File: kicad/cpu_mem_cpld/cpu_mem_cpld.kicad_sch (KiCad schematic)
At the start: 47 parts, among them CON1 BARREL_JACK, J1 USB, J3 DB9, SW1 SW_PUSH, U1 W65C02SxPL, U10 74HC245, U11 16550, U13 MAX232, U2 XC95108PC84, U3 28C256, U4 IS61C5128AS-25QLI, U5 74LS06, U6 LM555N, U9 74HC245, X1 OSC, X2 OSC

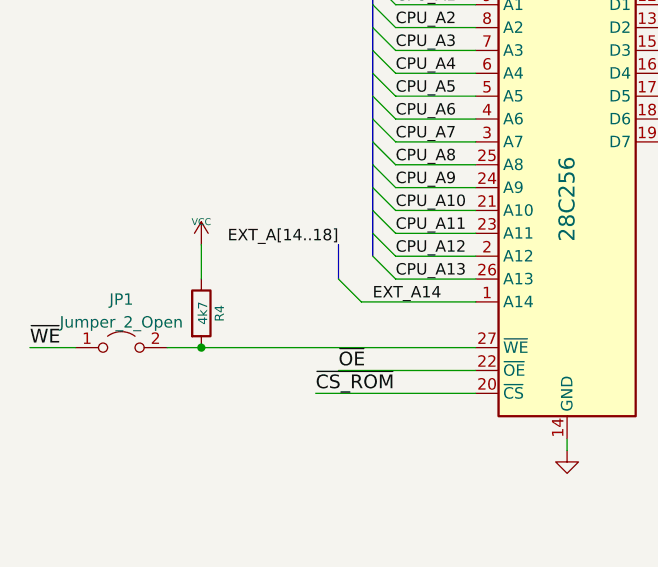
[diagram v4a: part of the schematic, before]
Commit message: eeprom rw jumper
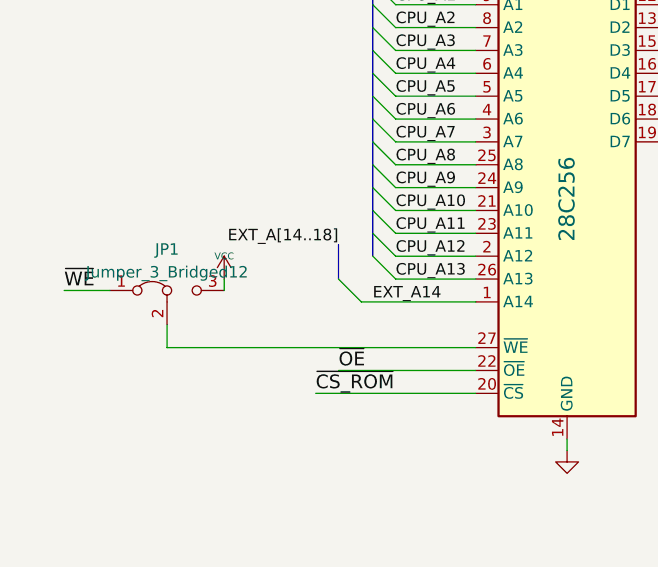
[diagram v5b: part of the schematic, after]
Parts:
- removed JP1: Jumper_2_Open, Connector_PinHeader_2.54mm:PinHeader_2x01_P2.54mm_Vertical, symbol Jumper:Jumper_2_Open
- removed R4: 4k7, Resistor_THT:R_Axial_DIN0204_L3.6mm_D1.6mm_P5.08mm_Horizontal, symbol Device:R
- added JP1: Jumper_3_Bridged12, Connector_PinHeader_2.54mm:PinHeader_1x03_P2.54mm_Vertical, symbol Jumper:Jumper_3_Bridged12
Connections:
- net VCC: now also JP1.3 (B)
- net ~{WE}: now also JP1.1 (A)
- net at U3.27 (~{WE}): now also JP1.2 (C)
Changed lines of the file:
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@@
   (junction (at 58.42 275.59) (diameter 0) (color 0 0 0 0)
   )
-  (junction (at 31.75 204.47) (diameter 0) (color 0 0 0 0)
-  )
   (junction (at 100.33 267.97) (diameter 0) (color 0 0 0 0)
   )
@@
     (stroke (width 0) (type default) (color 0 0 0 0))
   )
-  (wire (pts (xy 31.75 204.47) (xy 62.23 204.47))
+  (wire (pts (xy 27.94 204.47) (xy 62.23 204.47))
     (stroke (width 0) (type default) (color 0 0 0 0))
   )
@@
     (stroke (width 0) (type default) (color 0 0 0 0))
   )
+  (wire (pts (xy 27.94 201.93) (xy 27.94 204.47))
+    (stroke (width 0) (type default) (color 0 0 0 0))
+  )
   (wire (pts (xy 140.97 259.08) (xy 167.64 259.08))
     (stroke (width 0) (type default) (color 0 0 0 0))
@@
     (stroke (width 0) (type default) (color 0 0 0 0))
   )
-  (wire (pts (xy 31.75 193.04) (xy 31.75 196.85))
+  (wire (pts (xy 34.29 196.85) (xy 34.29 198.12))
     (stroke (width 0) (type default) (color 0 0 0 0))
   )
@@
     (stroke (width 0) (type default) (color 0 0 0 0))
   )
-  (wire (pts (xy 12.7 204.47) (xy 17.78 204.47))
+  (wire (pts (xy 16.51 198.12) (xy 21.59 198.12))
     (stroke (width 0) (type default) (color 0 0 0 0))
   )
@@
     (stroke (width 0) (type default) (color 0 0 0 0))
   )
-  (wire (pts (xy 27.94 204.47) (xy 31.75 204.47))
-    (stroke (width 0) (type default) (color 0 0 0 0))
-  )
   (wire (pts (xy 176.53 26.67) (xy 173.99 26.67))
     (stroke (width 0) (type default) (color 0 0 0 0))
@@
     (effects (font (size 1.524 1.524)) (justify right bottom))
   )
-  (label "~{WE}" (at 12.7 204.47 0)
+  (label "~{WE}" (at 16.51 198.12 0)
     (effects (font (size 1.524 1.524)) (justify left bottom))
   )
@@
     (pin "2")
   )
-  (symbol (lib_id "power:VCC") (at 31.75 193.04 0) (unit 1)
+  (symbol (lib_id "power:VCC") (at 34.29 196.85 0) (unit 1)
     (in_bom yes) (on_board yes)
-    (property "Reference" "#PWR013" (id 0) (at 31.75 190.5 0)
+    (property "Reference" "#PWR013" (id 0) (at 34.29 194.31 0)
       (effects (font (size 0.762 0.762)) hide)
     )
-    (property "Value" "VCC" (id 1) (at 31.75 190.5 0)
+    (property "Value" "VCC" (id 1) (at 34.29 194.31 0)
       (effects (font (size 0.762 0.762)))
     )
-    (property "Footprint" "" (id 2) (at 31.75 193.04 0)
+    (property "Footprint" "" (id 2) (at 34.29 196.85 0)
       (effects (font (size 1.524 1.524)))
     )
-    (property "Datasheet" "" (id 3) (at 31.75 193.04 0)
+    (property "Datasheet" "" (id 3) (at 34.29 196.85 0)
       (effects (font (size 1.524 1.524)))
     )
@@
     (pin "2")
   )
-  (symbol (lib_id "Device:R") (at 31.75 200.66 0) (unit 1)
-    (in_bom yes) (on_board yes)
-    (property "Reference" "R4" (id 0) (at 33.782 200.66 90)
-      (effects (font (size 1.016 1.016)))
-    )
-    (property "Value" "4k7" (id 1) (at 31.9278 200.6346 90)
-      (effects (font (size 1.016 1.016)))
-    )
-    (property "Footprint" "Resistor_THT:R_Axial_DIN0204_L3.6mm_D1.6mm_P5.08mm_Horizontal" (id 2) (at 29.972 200.66 90)
-      (effects (font (size 1.27 1.27)) hide)
-    )
-    (property "Datasheet" "~" (id 3) (at 31.75 200.66 0)
-      (effects (font (size 1.27 1.27)) hide)
-    )
-    (pin "1")
-    (pin "2")
-  )
   (symbol (lib_id "Device:R") (at 215.9 215.9 0) (unit 1)
     (in_bom yes) (on_board yes)
@@
     (pin "2")
   )
+  (symbol (lib_id "Jumper:Jumper_3_Bridged12") (at 27.94 198.12 0) (unit 1)
+    (in_bom yes) (on_board yes) (fields_autoplaced)
+    (property "Reference" "JP1" (id 0) (at 27.94 193.556 0))
+    (property "Value" "Jumper_3_Bridged12" (id 1) (at 27.94 196.0929 0))
+    (property "Footprint" "Connector_PinHeader_2.54mm:PinHeader_1x03_P2.54mm_Vertical" (id 2) (at 27.94 198.12 0)
+      (effects (font (size 1.27 1.27)) hide)
+    )
+    (property "Datasheet" "~" (id 3) (at 27.94 198.12 0)
+      (effects (font (size 1.27 1.27)) hide)
+    )
+    (pin "1")
+    (pin "2")
+    (pin "3")
+  )
   (symbol (lib_id "power:GND") (at 342.9 82.55 0) (mirror y) (unit 1)
     (in_bom yes) (on_board yes)
@@
     (pin "1")
   )
-  (symbol (lib_id "Jumper:Jumper_2_Open") (at 22.86 204.47 0) (unit 1)
-    (in_bom yes) (on_board yes) (fields_autoplaced)
-    (property "Reference" "JP1" (id 0) (at 22.86 199.1192 0))
-    (property "Value" "Jumper_2_Open" (id 1) (at 22.86 201.6561 0))
-    (property "Footprint" "Connector_PinHeader_2.54mm:PinHeader_2x01_P2.54mm_Vertical" (id 2) (at 22.86 204.47 0)
-      (effects (font (size 1.27 1.27)) hide)
-    )
-    (property "Datasheet" "~" (id 3) (at 22.86 204.47 0)
-      (effects (font (size 1.27 1.27)) hide)
-    )
-    (pin "1")
-    (pin "2")
-  )
   (symbol (lib_id "power:VCC") (at 367.03 137.16 0) (unit 1)
     (in_bom yes) (on_board yes)
@@
       (reference "J3") (unit 1) (value "DB9") (footprint "Connector_Dsub:DSUB-9_Male_Horizontal_P2.77x2.84mm_EdgePinOffset4.94mm_Housed_MountingHolesOffset7.48mm")
     )
-    (path "/b11517e7-c73e-41e7-81e8-b92d482d3709"
-      (reference "JP1") (unit 1) (value "Jumper_2_Open") (footprint "Connector_PinHeader_2.54mm:PinHeader_2x01_P2.54mm_Vertical")
+    (path "/73c8d8b3-21da-4d13-a537-b88a77632423"
+      (reference "JP1") (unit 1) (value "Jumper_3_Bridged12") (footprint "Connector_PinHeader_2.54mm:PinHeader_1x03_P2.54mm_Vertical")
     )
     (path "/00000000-0000-0000-0000-000062aa2d6c"
@@
       (reference "R3") (unit 1) (value "3k3") (footprint "Resistor_THT:R_Axial_DIN0204_L3.6mm_D1.6mm_P5.08mm_Horizontal")
     )
-    (path "/02cd4006-0b38-45e5-a021-fce1decf54d3"
-      (reference "R4") (unit 1) (value "4k7") (footprint "Resistor_THT:R_Axial_DIN0204_L3.6mm_D1.6mm_P5.08mm_Horizontal")
-    )
     (path "/00000000-0000-0000-0000-000054136b39"

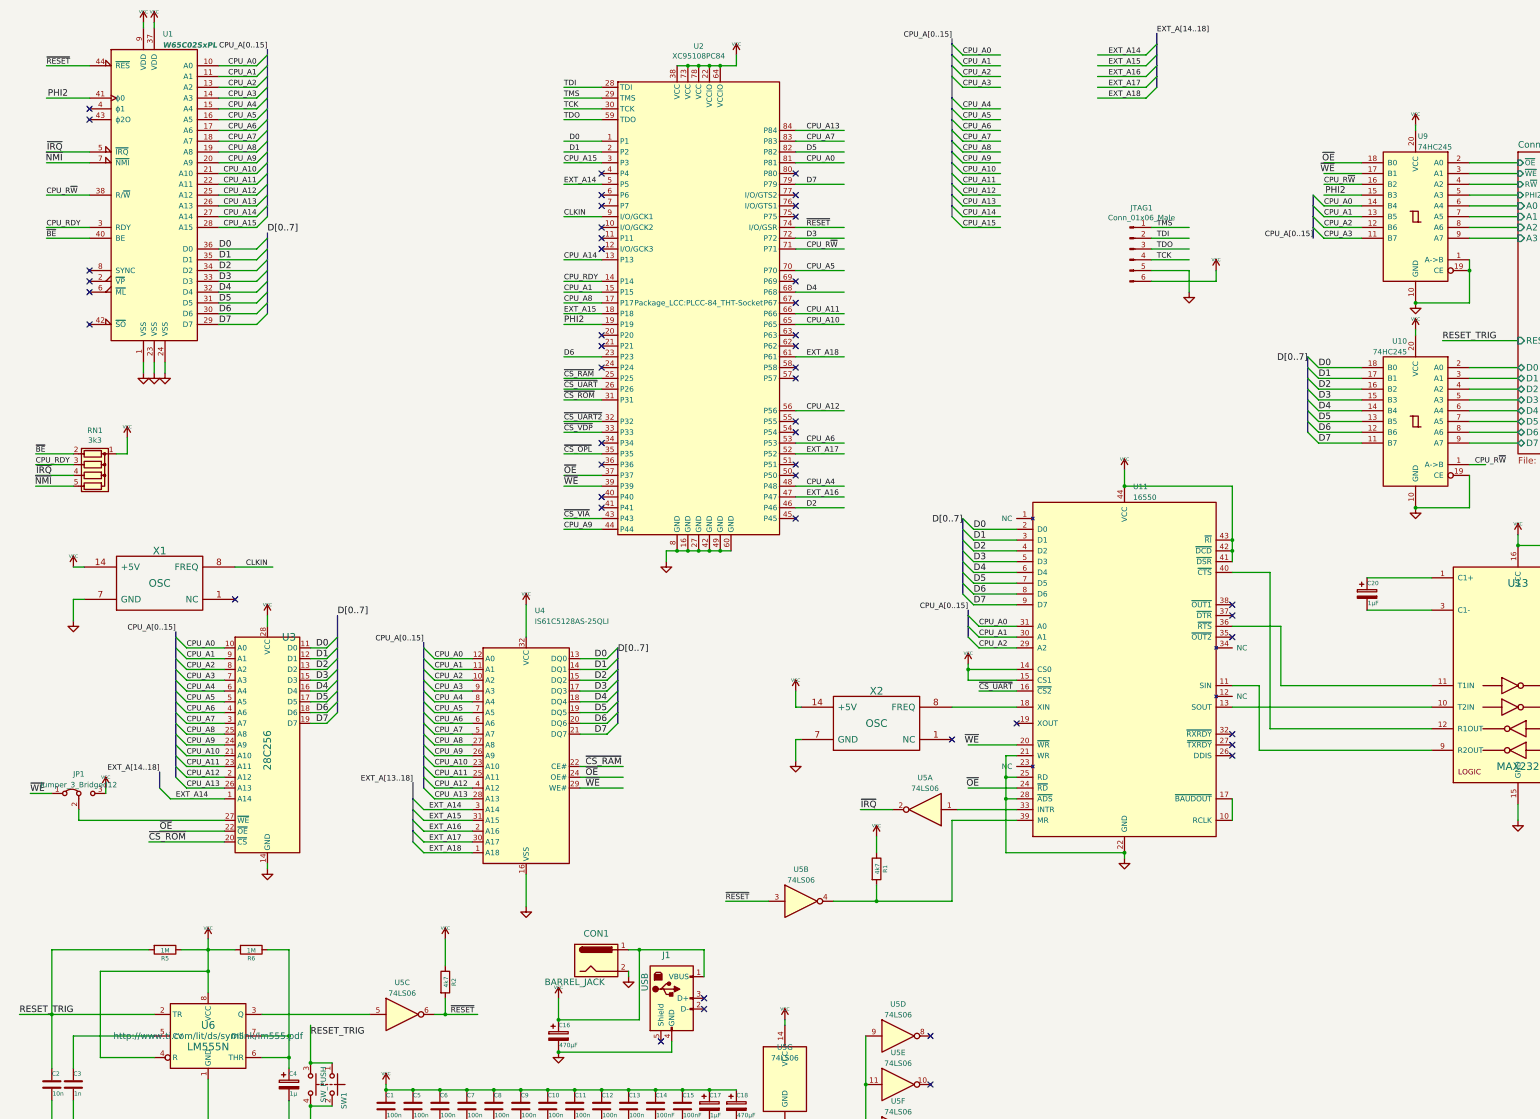
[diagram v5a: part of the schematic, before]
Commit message: cleanup autorouted traces
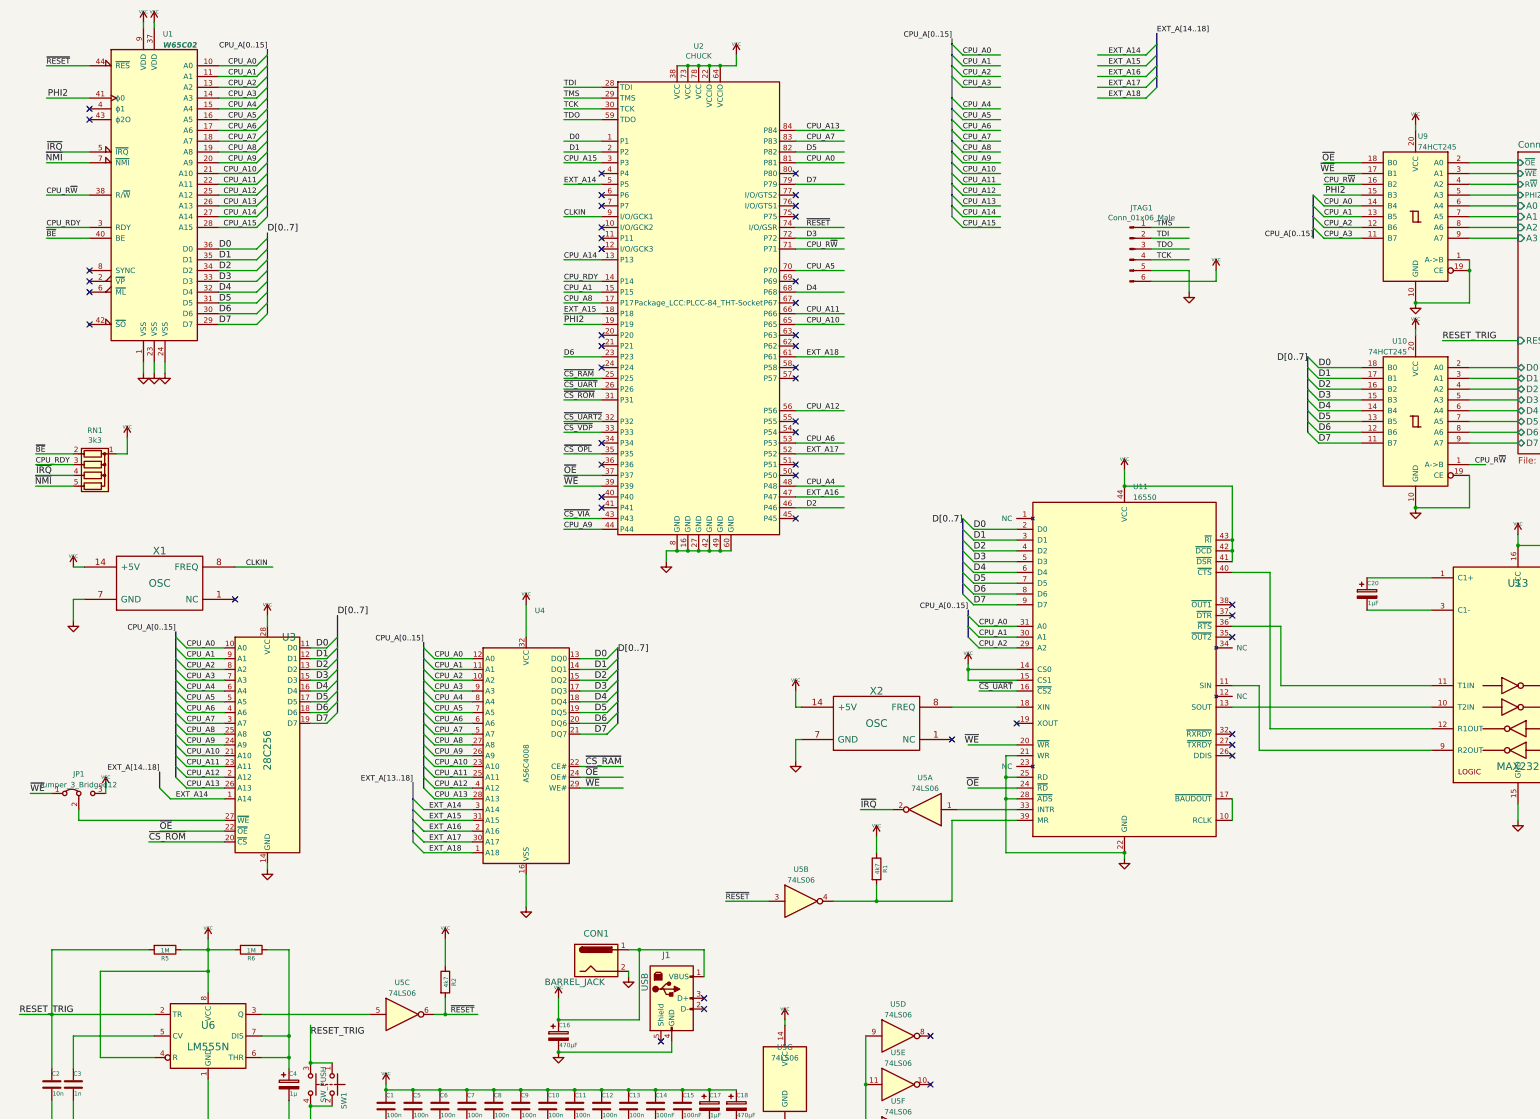
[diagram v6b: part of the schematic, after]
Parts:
- U1: value W65C02SxPL -> W65C02
- U10, U9: value 74HC245 -> 74HCT245
- U2: value XC95108PC84 -> CHUCK
- U4: value IS61C5128AS-25QLI -> AS6C4008
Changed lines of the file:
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@@
     )
     (property "Datasheet" "http://www.ti.com/lit/ds/symlink/lm555.pdf" (id 3) (at 58.42 255.27 0)
-      (effects (font (size 1.524 1.524)))
+      (effects (font (size 1.524 1.524)) hide)
     )
     (pin "1")
@@
     (in_bom yes) (on_board yes)
     (property "Reference" "U2" (id 0) (at 173.99 22.0726 0))
-    (property "Value" "XC95108PC84" (id 1) (at 173.99 24.384 0))
+    (property "Value" "CHUCK" (id 1) (at 173.99 24.384 0))
     (property "Footprint" "Package_LCC:PLCC-84_THT-Socket" (id 2) (at 173.99 82.55 0))
     (property "Datasheet" "xilinx/xc95108.pdf" (id 3) (at 173.99 82.55 0)
@@
       (effects (font (size 1.27 1.27)) (justify left))
     )
-    (property "Value" "W65C02SxPL" (id 1) (at 47.7394 21.8069 0)
+    (property "Value" "W65C02" (id 1) (at 47.7394 21.8069 0)
       (effects (font (size 1.27 1.27) bold italic) (justify left))
     )
@@
   )
   (symbol (lib_id "Memory_RAM:AS6C4008-55PCN") (at 133.35 189.23 0) (unit 1)
-    (in_bom yes) (on_board yes) (fields_autoplaced)
+    (in_bom yes) (on_board yes)
     (property "Reference" "U4" (id 0) (at 135.3694 155.0502 0)
       (effects (font (size 1.27 1.27)) (justify left))
     )
-    (property "Value" "IS61C5128AS-25QLI" (id 1) (at 135.3694 157.5871 0)
+    (property "Value" "AS6C4008" (id 1) (at 133.35 195.58 90)
       (effects (font (size 1.27 1.27)) (justify left))
     )
@@
       (effects (font (size 1.27 1.27)) (justify right))
     )
-    (property "Value" "74HC245" (id 1) (at 343.4206 45.8271 0)
+    (property "Value" "74HCT245" (id 1) (at 343.4206 45.8271 0)
       (effects (font (size 1.27 1.27)) (justify right))
     )
@@
       (effects (font (size 1.27 1.27)) (justify left))
     )
-    (property "Value" "74HC245" (id 1) (at 340.8806 94.0871 0)
+    (property "Value" "74HCT245" (id 1) (at 340.8806 94.0871 0)
       (effects (font (size 1.27 1.27)) (justify left))
     )
@@
     )
     (path "/06e52be3-aba9-4030-8cbf-c06e7f2efac9"
-      (reference "U1") (unit 1) (value "W65C02SxPL") (footprint "Package_LCC:PLCC-44_THT-Socket")
+      (reference "U1") (unit 1) (value "W65C02") (footprint "Package_LCC:PLCC-44_THT-Socket")
     )
     (path "/00000000-0000-0000-0000-000061437317"
-      (reference "U2") (unit 1) (value "XC95108PC84") (footprint "Package_LCC:PLCC-84_THT-Socket")
+      (reference "U2") (unit 1) (value "CHUCK") (footprint "Package_LCC:PLCC-84_THT-Socket")
     )
     (path "/00000000-0000-0000-0000-00005413ddc9"
@@
     )
     (path "/4705adbd-fd46-491d-b0da-c83c94b713f2"
-      (reference "U4") (unit 1) (value "IS61C5128AS-25QLI") (footprint "Package_DIP:DIP-32_W15.24mm_LongPads")
+      (reference "U4") (unit 1) (value "AS6C4008") (footprint "Package_DIP:DIP-32_W15.24mm_LongPads")
     )
     (path "/341459f0-40e4-4542-8af3-3b1a6b57c985"
@@
     )
     (path "/99fe5539-27bd-4115-9ac3-c6fdc6564453"
-      (reference "U9") (unit 1) (value "74HC245") (footprint "Package_DIP:DIP-20_W7.62mm_LongPads")
+      (reference "U9") (unit 1) (value "74HCT245") (footprint "Package_DIP:DIP-20_W7.62mm_LongPads")
     )
     (path "/c7a609e4-f868-4561-8e9a-f1e9ed27edb9"
-      (reference "U10") (unit 1) (value "74HC245") (footprint "Package_DIP:DIP-20_W7.62mm_LongPads")
+      (reference "U10") (unit 1) (value "74HCT245") (footprint "Package_DIP:DIP-20_W7.62mm_LongPads")
     )
     (path "/f4aa2c34-c56a-4ad1-8aae-7adffd1a3bb0"

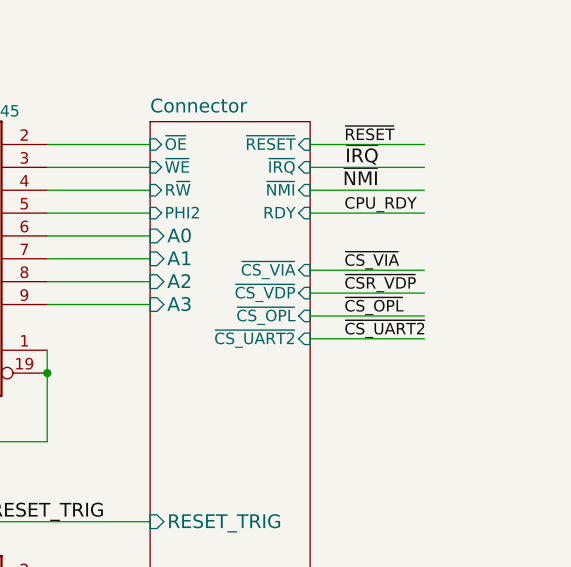
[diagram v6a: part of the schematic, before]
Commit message: fix missing cs vdp
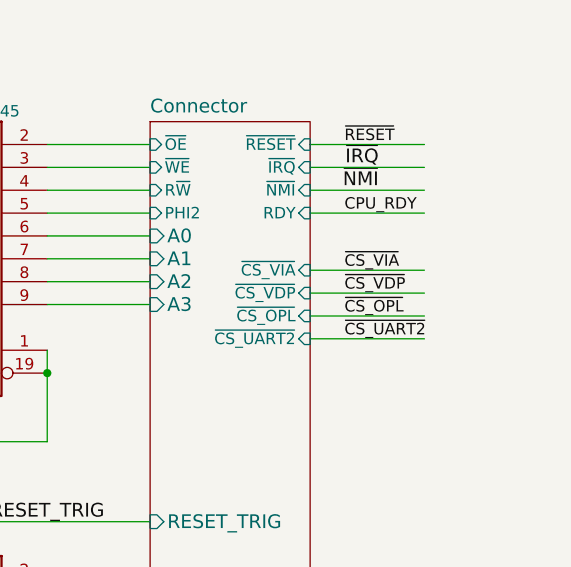
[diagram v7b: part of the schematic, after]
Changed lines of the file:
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@@
     (effects (font (size 1.27 1.27)) (justify left bottom))
   )
-  (label "~{CSR_VDP}" (at 388.62 66.04 0)
+  (label "~{CS_VDP}" (at 388.62 66.04 0)
     (effects (font (size 1.27 1.27)) (justify left bottom))
   )
